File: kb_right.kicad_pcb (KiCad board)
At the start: 2 copper layers, 208.8 x 117.5 mm, 171 parts, among them J1 10029449-001RLF, SW0 RotaryEncoder_Switch

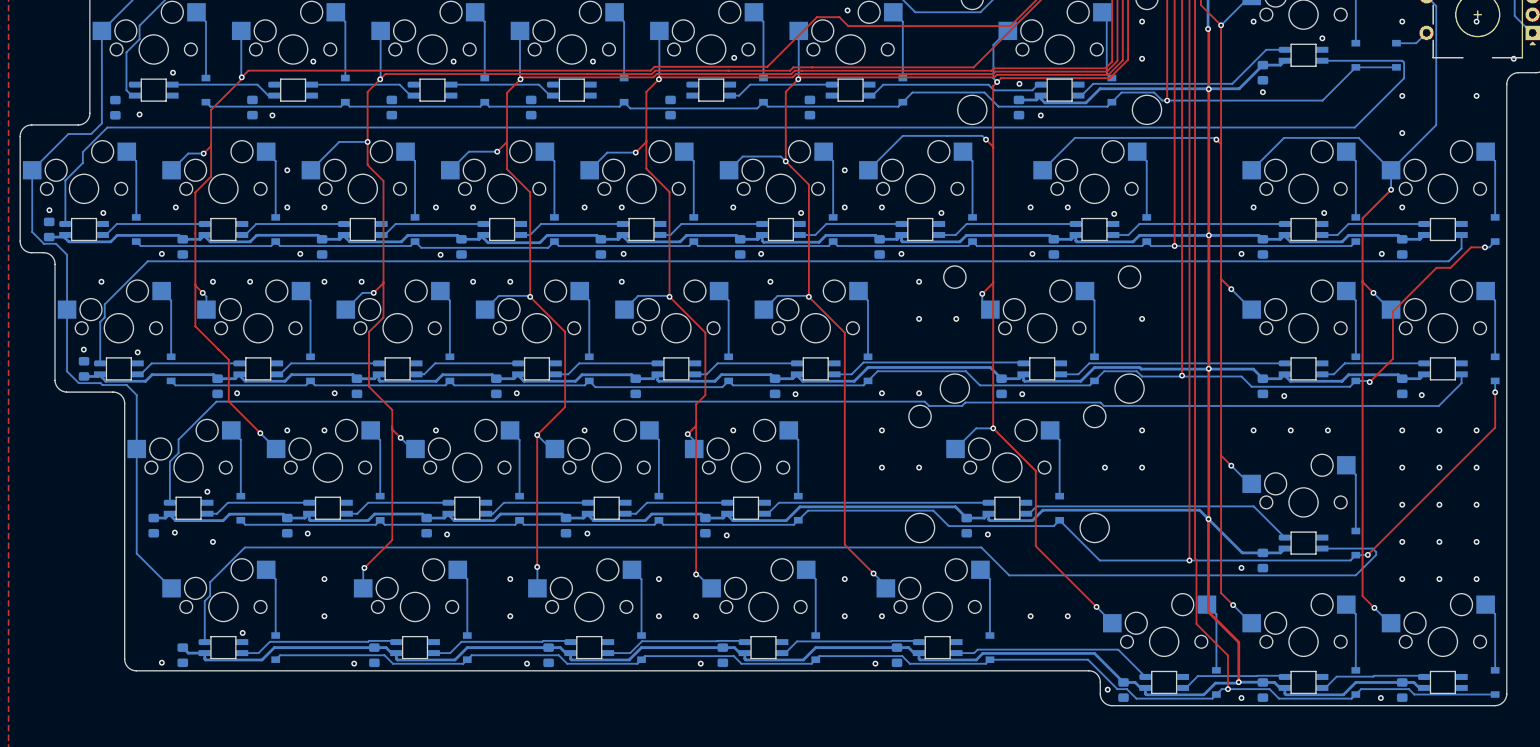
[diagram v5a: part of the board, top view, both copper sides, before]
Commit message: fixed sk6812 routing
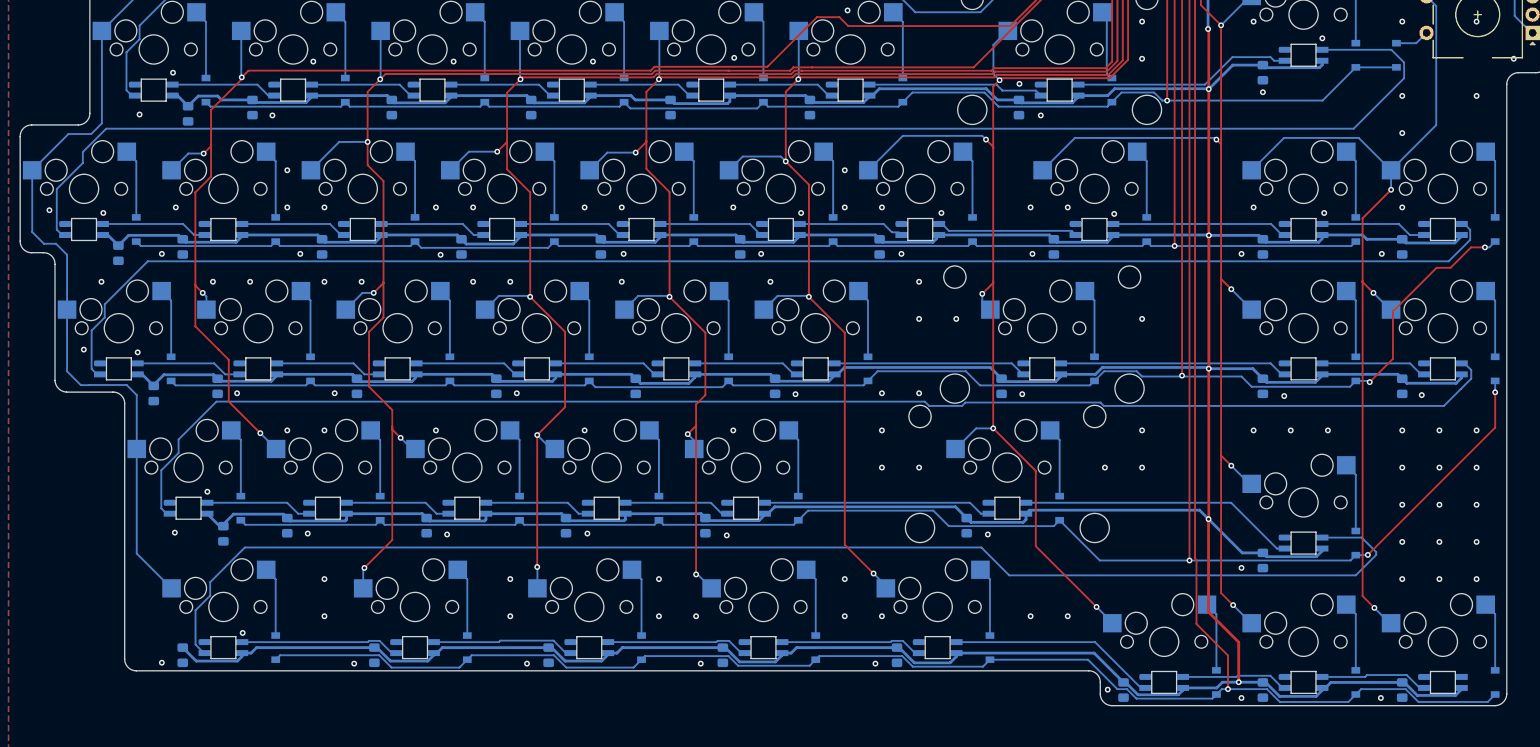
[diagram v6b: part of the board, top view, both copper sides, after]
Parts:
- moved C119 10.1 mm to (58.4, 110.7), turned to -90 degrees
- moved C109 10.0 mm to (53.6, 91.6), turned to -90 degrees
- moved C101 9.97 mm to (63.1, 72.5)
- moved C128 9.59 mm to (67.9, 129.9)
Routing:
- net +5V: track 1892.9 -> 1016.8 mm
- net GND: track 410.0 -> 1.56 mm, vias 140 -> 139
- net Net-(D108-Pad2): track 0.00 -> 212.4 mm
- net Net-(D118-Pad2): track 0.00 -> 204.2 mm
- net Net-(D127-Pad2): track 0.00 -> 195.8 mm
- net Net-(D134-Pad2): track 0.00 -> 183.8 mm
- net Net-(D133-Pad2): track 0.00 -> 38.0 mm
- net Net-(D132-Pad2): track 0.00 -> 31.2 mm
- net Net-(D125-Pad2): track 0.00 -> 31.2 mm
- net Net-(D107-Pad2): track 0.00 -> 30.0 mm
- net Net-(D139-Pad2): track 0.00 -> 28.5 mm
- net Net-(D124-Pad2): track 0.00 -> 26.5 mm
- net Net-(D106-Pad2): track 0.00 -> 24.1 mm
- net Net-(D116-Pad2): track 0.00 -> 23.1 mm
- net Net-(D135-Pad2): track 0.00 -> 21.9 mm
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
